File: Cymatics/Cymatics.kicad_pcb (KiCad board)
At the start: 2 copper layers, 65 x 70 mm, 72 parts, among them IC1 LMV358IDR, IC2 MAX7403CSA+, IC3 LMV358IDR, IC4 LMV358IDR, IC5 MAX7403CSA+, J1 Screw_Terminal_01x03, J10 Screw_Terminal_01x04, J11 Screw_Terminal_01x05, J12 Screw_Terminal_01x02, J13 Screw_Terminal_01x02, J15 Screw_Terminal_01x02, J16 Screw_Terminal_01x03, J17 Screw_Terminal_01x02, J18 Screw_Terminal_01x06, J2 Screw_Terminal_01x02, J3 Screw_Terminal_01x03, J4 Screw_Terminal_01x03, J5 Screw_Terminal_01x02, J6 Conn_01x16_Socket, J7 Conn_01x12_Socket, J8 Screw_Terminal_01x04, J9 Screw_Terminal_01x02, U1 SN74AHCT125DR, U2 MAX7480ESA+

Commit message: resolved all DRC errors
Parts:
- moved C9 0.50 mm to (124.5, 114.5)
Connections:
- J6 pad 10: unconnected-(J6-Pin_10-Pad10) -> EXT_CS
- J6 pad 15: EXT_CS -> unconnected-(J6-Pin_15-Pad15)
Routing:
- net EXT_CS: track 11.1 -> 21.6 mm, vias 1 -> 0
- net SCK: track 40.4 -> 39.6 mm
- net A2: track 44.8 -> 44.9 mm, vias 2 -> 3
- net GND: vias 36 -> 38
- net A3: vias 4 -> 5
- net A1: vias 0 -> 1
- net A0: vias 0 -> 1

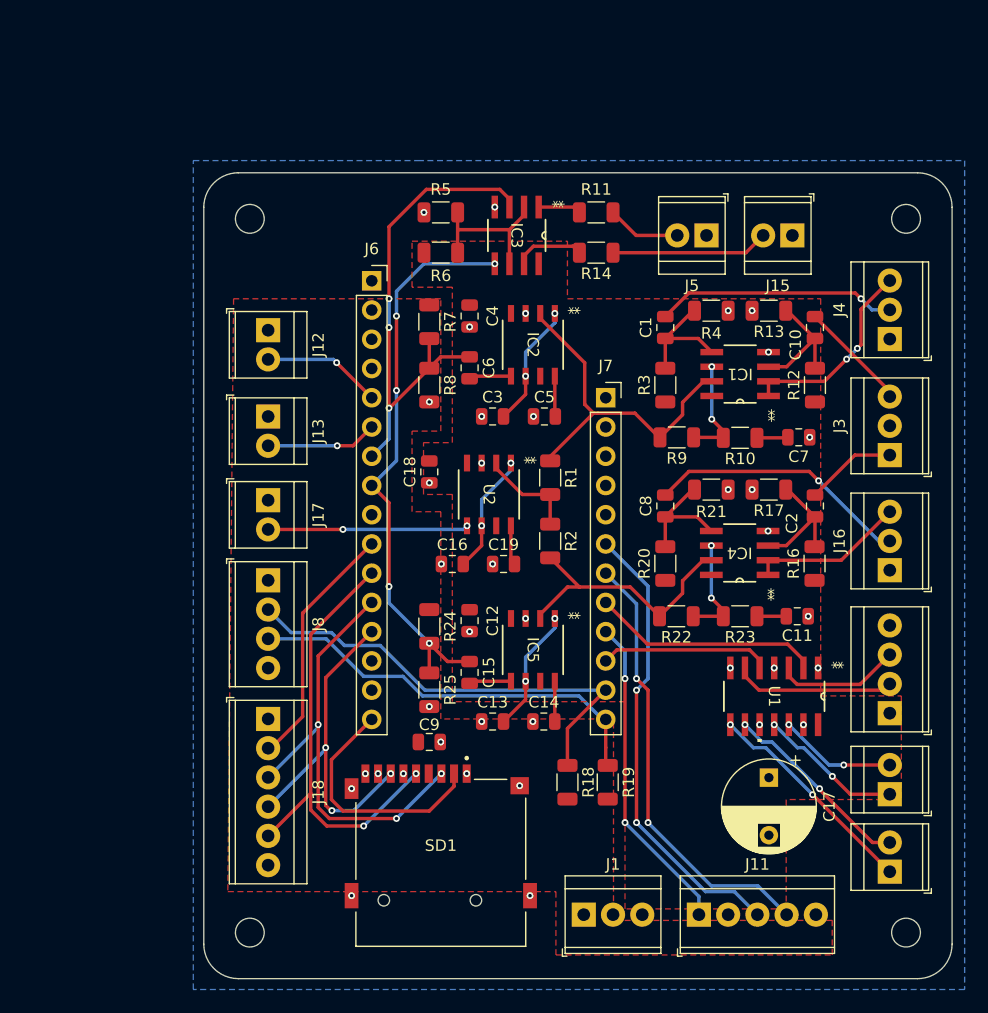
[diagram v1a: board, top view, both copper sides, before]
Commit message: added testpoints
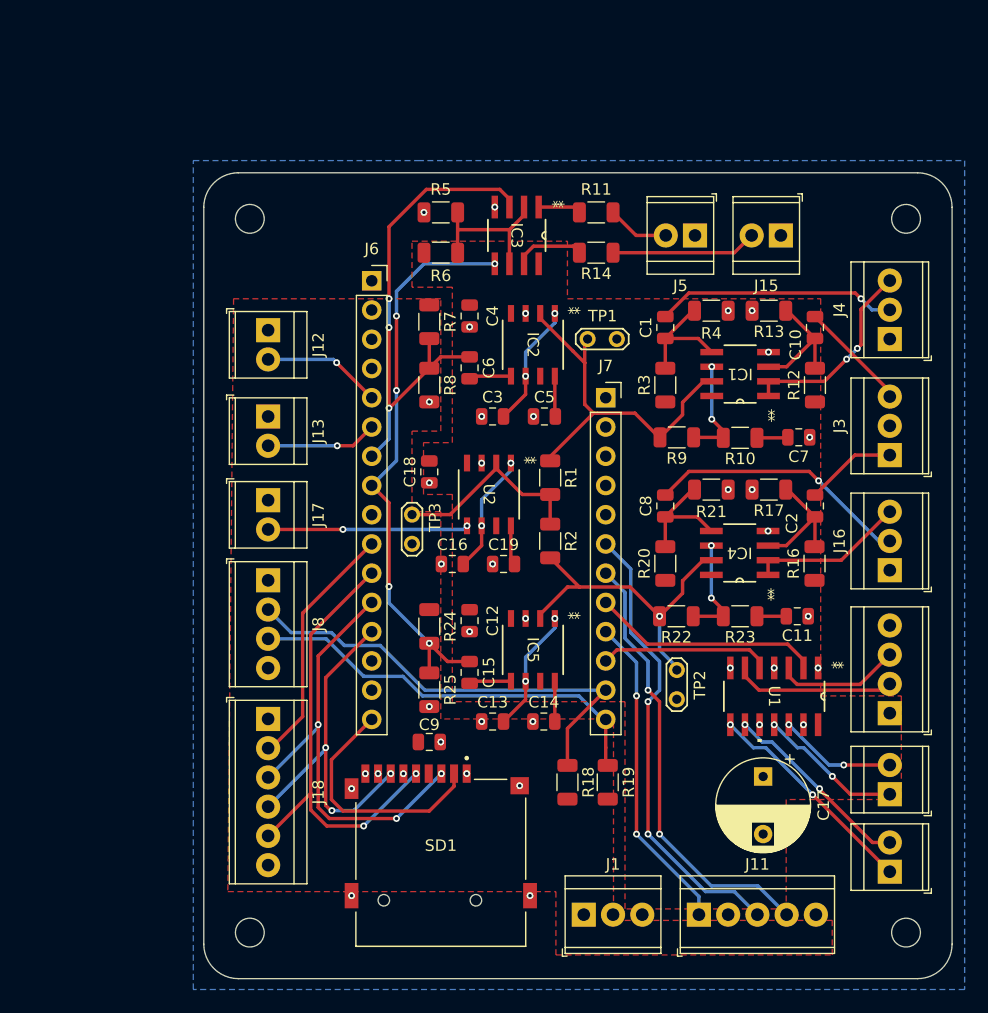
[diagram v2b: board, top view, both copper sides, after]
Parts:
- added TP1: TestPoint_2Pole, TestPoint:TestPoint_2Pads_Pitch2.54mm_Drill0.8mm, F.Cu at (138.2, 79.5)
- added TP2: TestPoint_2Pole, TestPoint:TestPoint_2Pads_Pitch2.54mm_Drill0.8mm, F.Cu at (146.0, 108.2)
- added TP3: TestPoint_2Pole, TestPoint:TestPoint_2Pads_Pitch2.54mm_Drill0.8mm, F.Cu at (123.0, 94.8)
- moved J15 1.00 mm to (155.0, 70.5)
- moved J5 1.00 mm to (147.6, 70.5)
- moved C17 0.51 mm to (153.5, 117.5)
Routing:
- net Net-(U2-IN): track 8.66 -> 17.6 mm
- net Net-(IC4-2OUT): track 23.5 -> 28.8 mm, vias 0 -> 1
- net Net-(IC1-2OUT): track 30.5 -> 32.7 mm
- net Net-(J5-Pin_2): track 6.41 -> 5.41 mm
- net Net-(J15-Pin_2): track 13.7 -> 12.7 mm

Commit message: testpoints update and terminal block labels
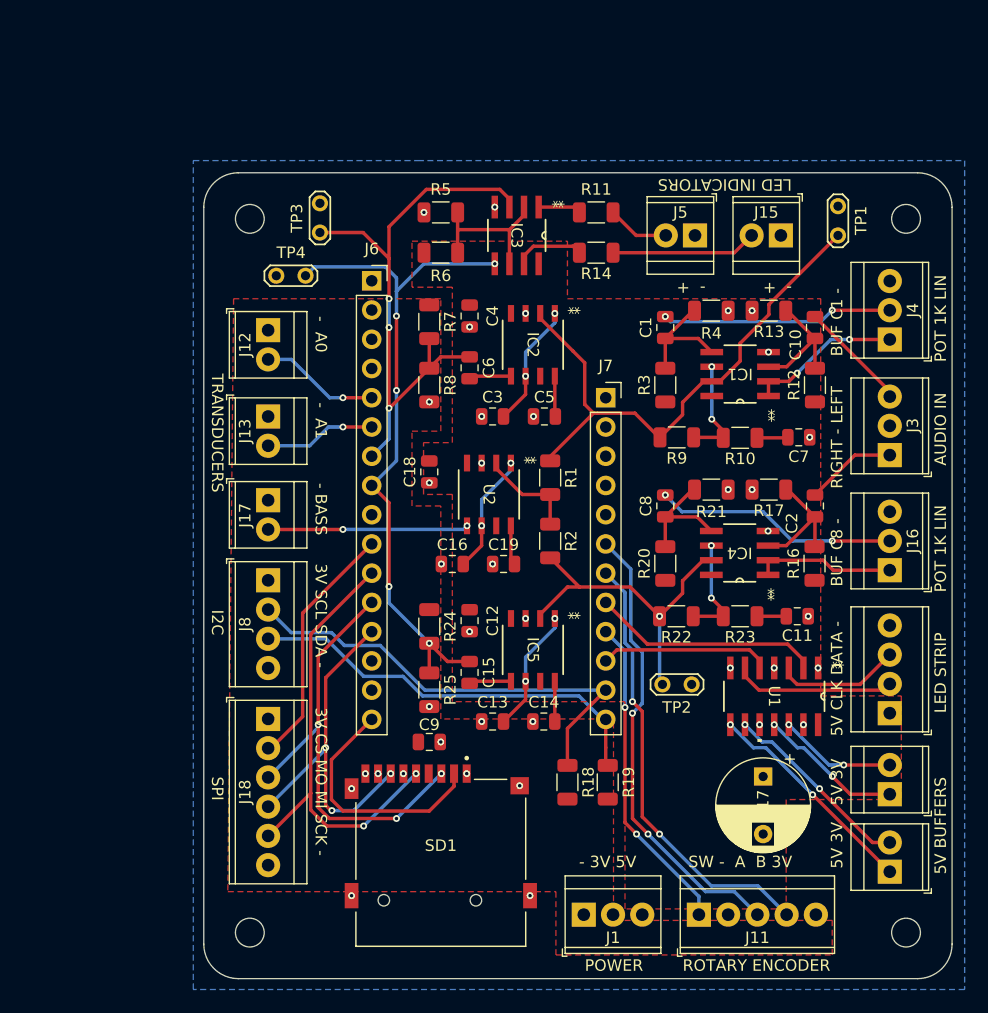
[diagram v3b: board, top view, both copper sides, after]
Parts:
- added TP4: TestPoint_2Pole, TestPoint:TestPoint_2Pads_Pitch2.54mm_Drill0.8mm, F.Cu at (113.8, 74.0)
- moved TP3 25.8 mm to (115.0, 70.2), turned to 90 degrees
- moved TP1 23.5 mm to (160.0, 70.5), turned to 90 degrees
- moved TP2 1.77 mm to (144.8, 109.5), turned to 0 degrees
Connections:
- J16 pad 1: GND -> Net-(IC4-1IN-)
- J16 pad 3: Net-(IC4-1IN-) -> GND
- J4 pad 1: GND -> Net-(IC1-1IN-)
- J4 pad 3: Net-(IC1-1IN-) -> GND
- TP3 pad 1: Net-(U2-IN) -> A2
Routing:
- net Net-(IC1-2OUT): track 32.7 -> 48.2 mm
- net A3: track 49.8 -> 59.6 mm
- net Net-(U2-IN): track 17.6 -> 8.66 mm
- net A2: track 44.9 -> 51.8 mm
- net Net-(IC1-1IN-): track 17.2 -> 13.3 mm
- net Net-(J16-Pin_2): track 22.9 -> 21.2 mm, vias 1 -> 2
- net Net-(IC4-1IN-): track 13.6 -> 12.2 mm
- net Net-(J4-Pin_2): track 21.0 -> 20.1 mm, vias 1 -> 2
- net Net-(IC4-2OUT): track 28.8 -> 29.5 mm
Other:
- board text added: "- +"
- board text added: "- 3V 5V"
- board text added: "- A0"
- board text added: "- A1"
- board text added: "- BASS"
- board text added: "3V CS MO MI SCK -"
- board text added: "3V SCL SDA -"
- board text added: "5V 3V"
- board text added: "5V BUFFERS"
- board text added: "5V CLK DATA -"
- board text added: "AUDIO IN"
- board text added: "BUF C1 -"
- board text added: "BUF C8 -"
- board text added: "I2C"
- board text added: "LED INDICATORS"
- board text added: "LED STRIP"
- board text added: "POT 1K LIN"
- board text added: "POWER"
- board text added: "RIGHT - LEFT"
- board text added: "ROTARY ENCODER"
- board text added: "SPI"
- board text added: "SW - A B 3V"
- board text added: "TRANSDUCERS"

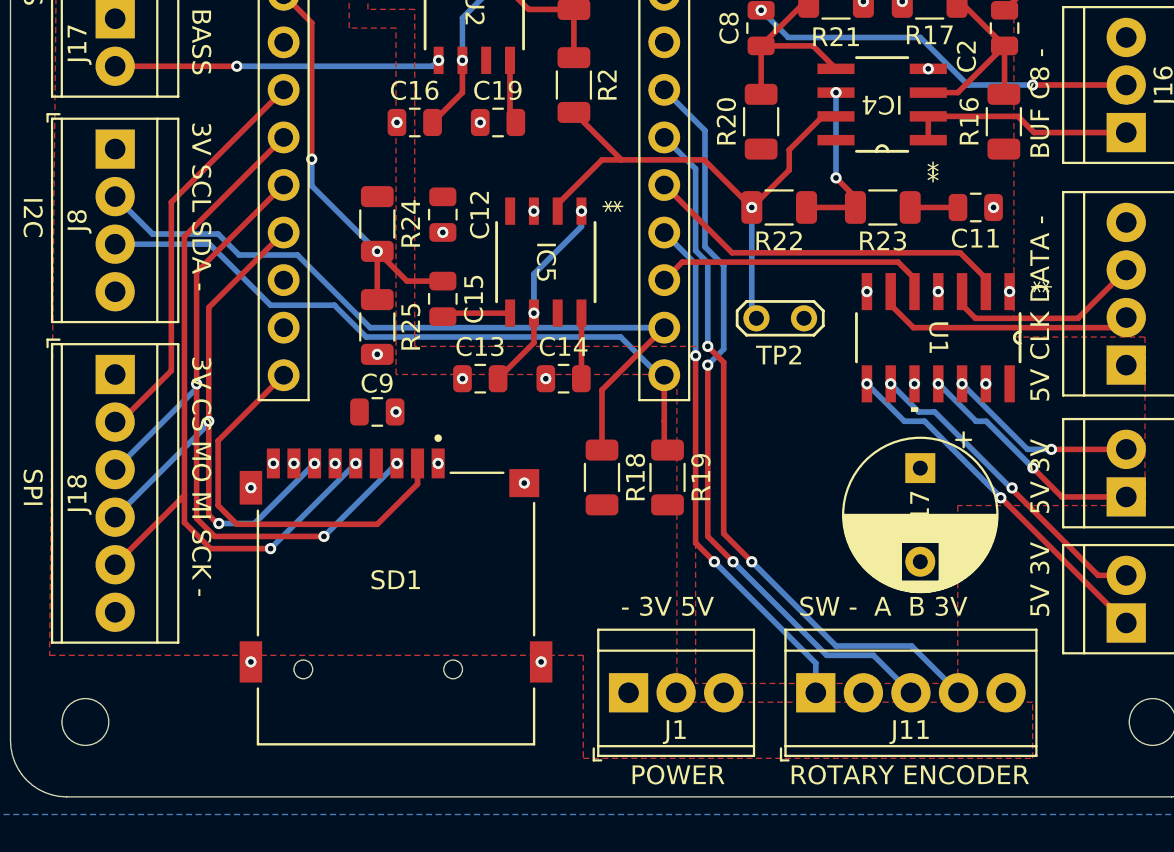
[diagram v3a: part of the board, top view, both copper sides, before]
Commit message: swizzled rotary encoder block
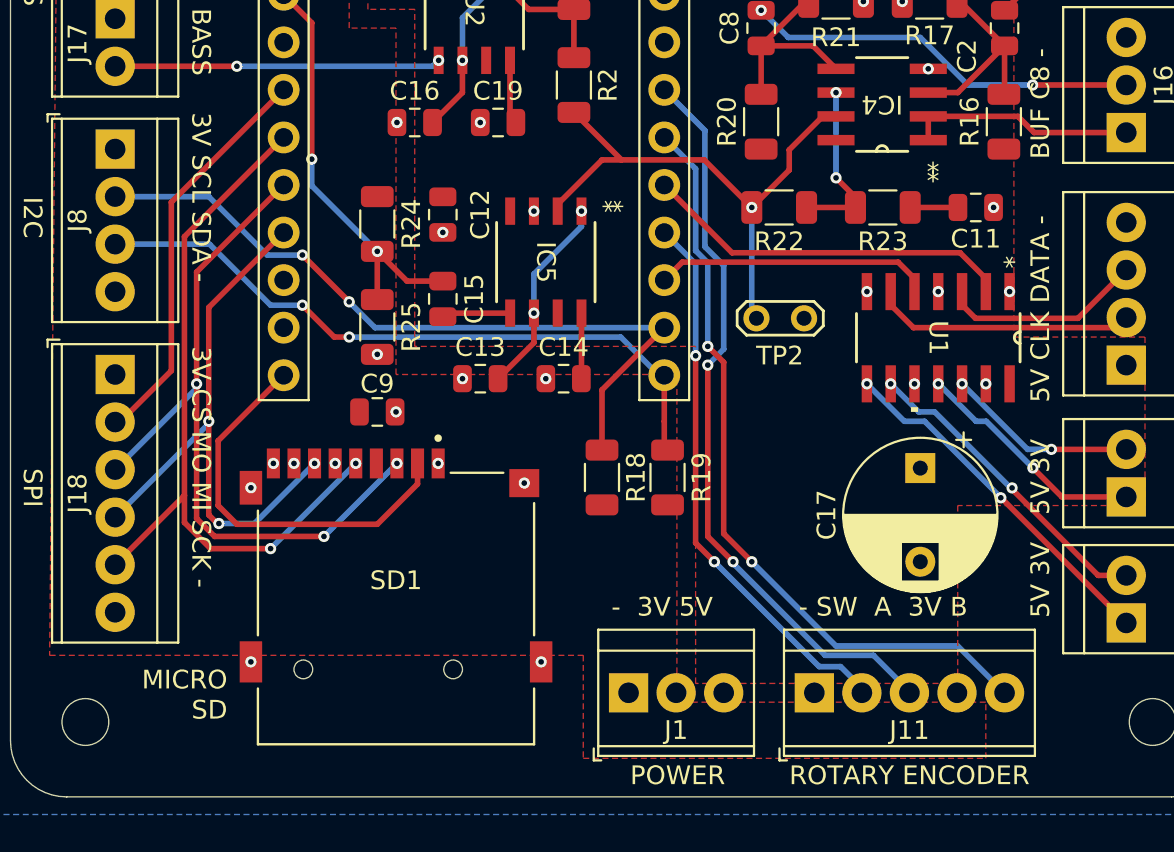
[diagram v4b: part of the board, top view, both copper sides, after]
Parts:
- moved J11 0.08 mm to (147.8, 129.5)
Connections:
- J11 pad 1: RE_SW1 -> GND
- J11 pad 2: GND -> RE_SW1
- J11 pad 4: RE_B -> 3V3
- J11 pad 5: 3V3 -> RE_B
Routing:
- net RE_B: track 38.5 -> 41.0 mm
- net RE_SW1: track 27.9 -> 29.6 mm
- net SDA: vias 0 -> 2
- net SCL: vias 0 -> 2
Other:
- board text added: "- SW A 3V B"
- board text added: "MICRO SD"
- board text removed: "SW - A B 3V"

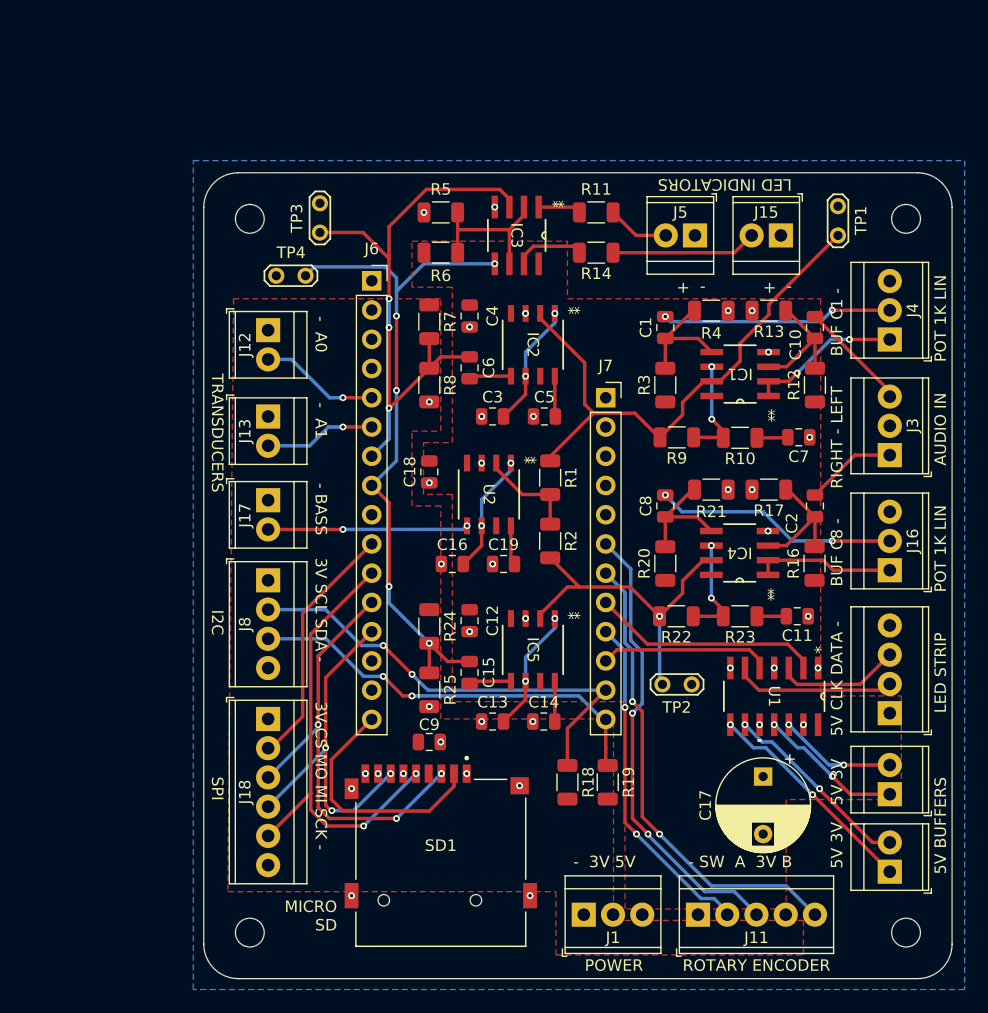
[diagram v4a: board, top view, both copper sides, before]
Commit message: new testpoint RCU-0C
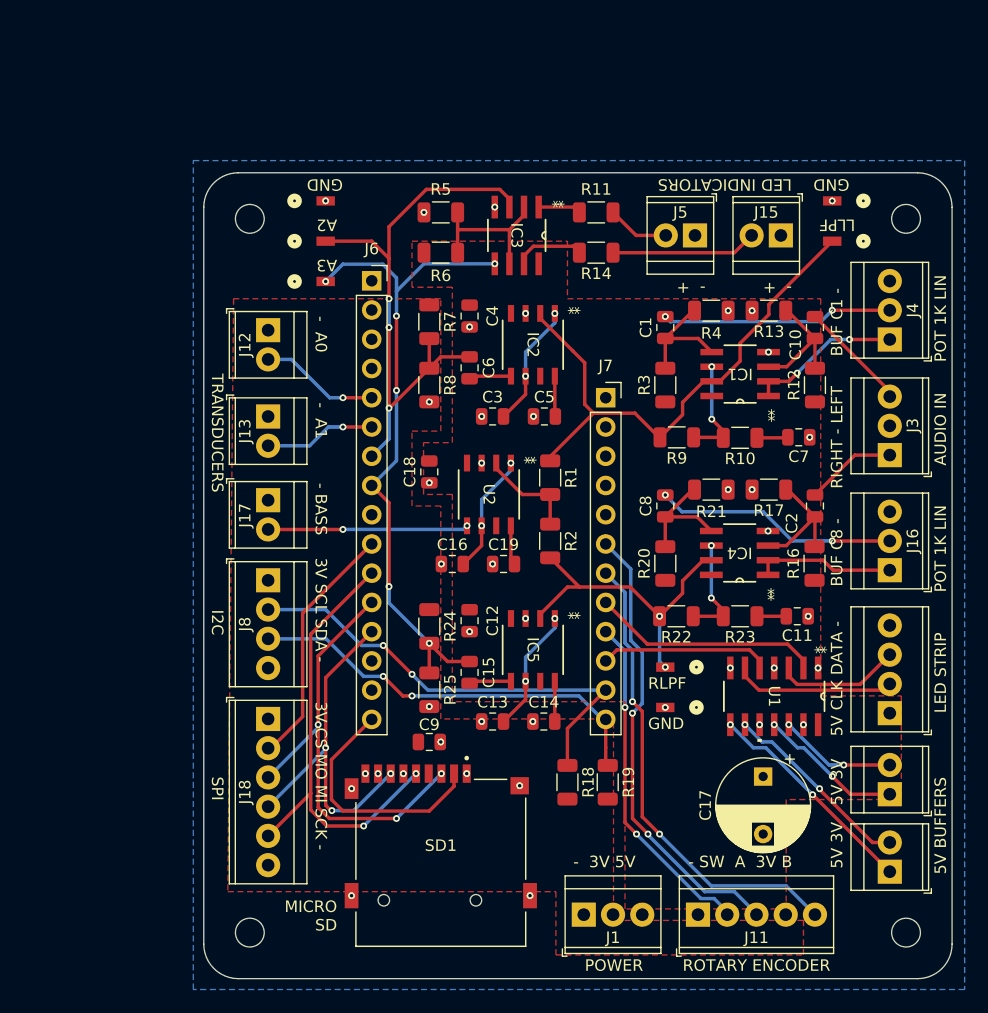
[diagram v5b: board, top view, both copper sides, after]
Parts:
- removed TP1, TP2, TP3, TP4: TestPoint_2Pole, TestPoint:TestPoint_2Pads_Pitch2.54mm_Drill0.8mm
- added J14: RCU-0C, RCU-0C:CONN1_RCU-0C_TEC, F.Cu at (159.5, 71.0)
- added J19: RCU-0C, RCU-0C:CONN1_RCU-0C_TEC, F.Cu at (159.5, 67.5)
- added J20: RCU-0C, RCU-0C:CONN1_RCU-0C_TEC, F.Cu at (145.0, 108.0)
- added J21: RCU-0C, RCU-0C:CONN1_RCU-0C_TEC, F.Cu at (145.0, 111.5)
- added J22: RCU-0C, RCU-0C:CONN1_RCU-0C_TEC, F.Cu at (115.5, 71.0)
- added J23: RCU-0C, RCU-0C:CONN1_RCU-0C_TEC, F.Cu at (115.5, 74.5)
- added J24: RCU-0C, RCU-0C:CONN1_RCU-0C_TEC, F.Cu at (115.5, 67.5)
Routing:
- net Net-(IC4-2OUT): track 29.5 -> 28.1 mm, vias 1 -> 2
- net A3: track 59.6 -> 58.2 mm, vias 5 -> 6
- net A2: track 51.8 -> 51.0 mm
- net Net-(IC1-2OUT): track 48.2 -> 47.5 mm
- net GND: vias 38 -> 41
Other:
- board text added: "A2"
- board text added: "A3"
- board text added: "GND"
- board text added: "LLPF"
- board text added: "RLPF"

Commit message: changes and Gerber Drill generate for order
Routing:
- net A2: track 51.0 -> 44.1 mm, vias 3 -> 4
- net A3: track 58.2 -> 57.4 mm
- net Net-(IC3-1IN-): track 13.5 -> 13.4 mm, vias 0 -> 4

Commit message: added cymatics label and ordered PCB and parts
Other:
- board text added: "CYMATICS FEB 2025"
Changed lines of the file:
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@@
 		(tags "resistor")
 		(property "Reference" "R18"
-			(at 0 -1.82 90)
+			(at 4 0 90)
 			(layer "F.SilkS")
 			(effects
@@
 		(tags "resistor")
 		(property "Reference" "R19"
-			(at 0 -1.82 90)
+			(at 4 0 90)
 			(layer "F.SilkS")
 			(effects
@@
 			)
 			(justify left bottom)
+		)
+	)
+	(gr_text "CYMATICS\nFEB\n2025"
+		(at 141.5 120.5 0)
+		(layer "F.SilkS")
+		(effects
+			(font
+				(size 1.25 1.25)
+				(thickness 0.25)
+				(bold yes)
+			)
+			(justify left bottom)
